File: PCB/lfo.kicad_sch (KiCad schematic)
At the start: 12 parts, among them J4 LFO, U2 LM324

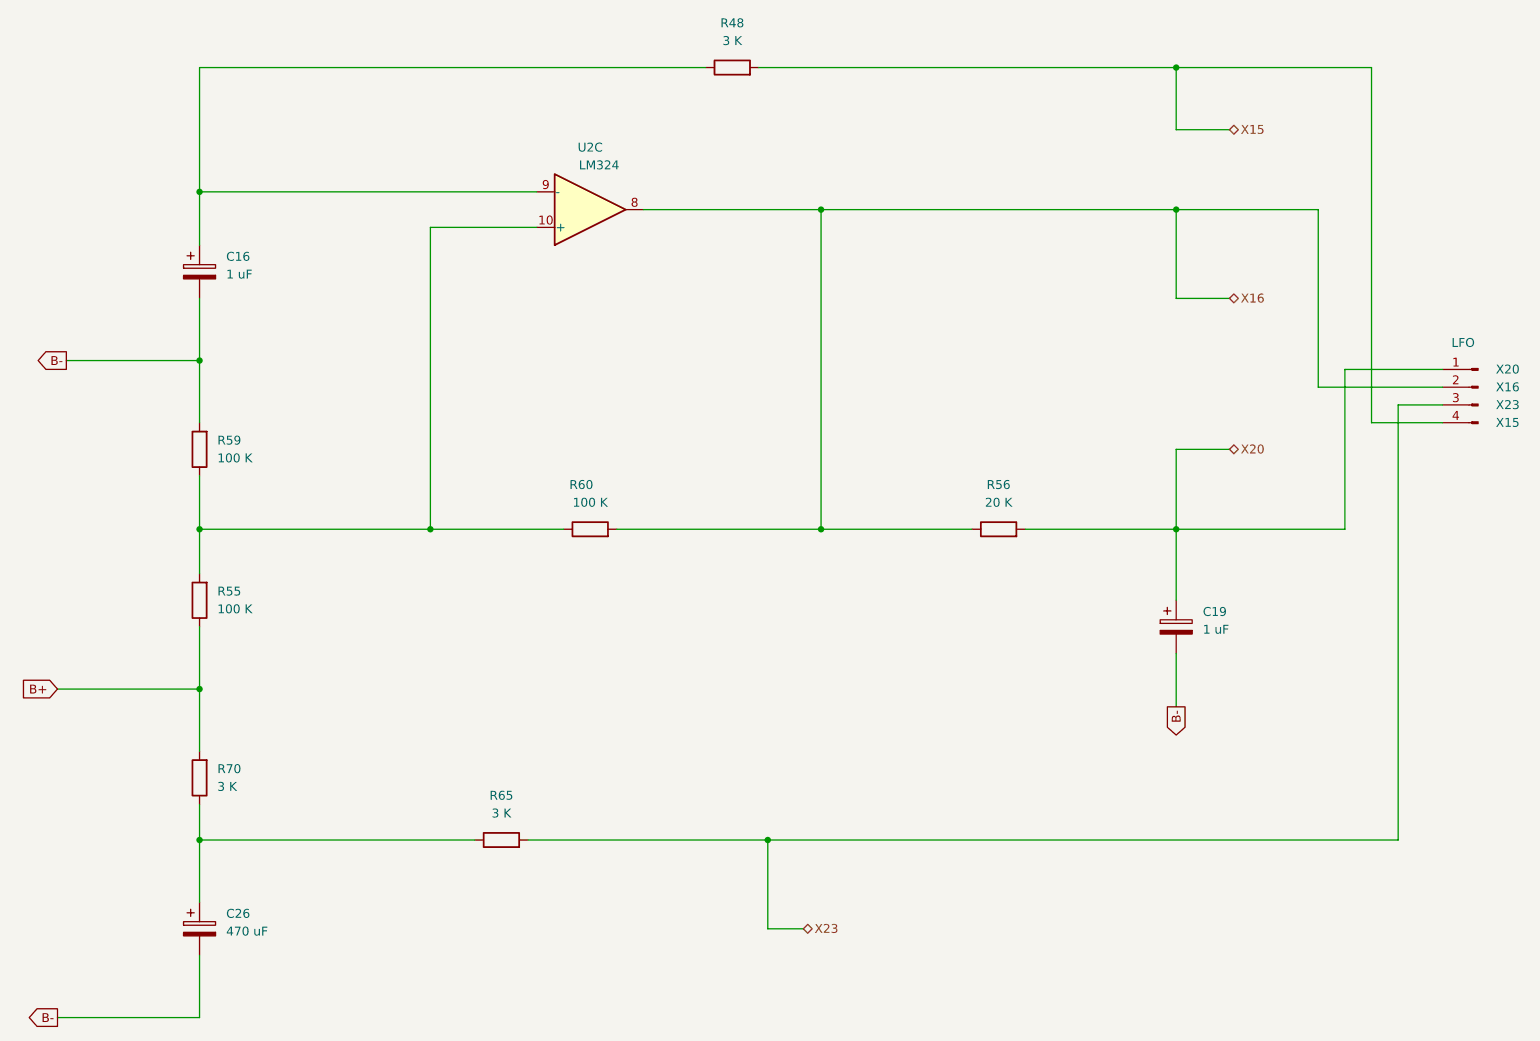
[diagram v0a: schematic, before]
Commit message: Change TO-92 transistors to wide package to avoid shorting during soldering
Added B- hole for speaker
Added more vias to shorten traces
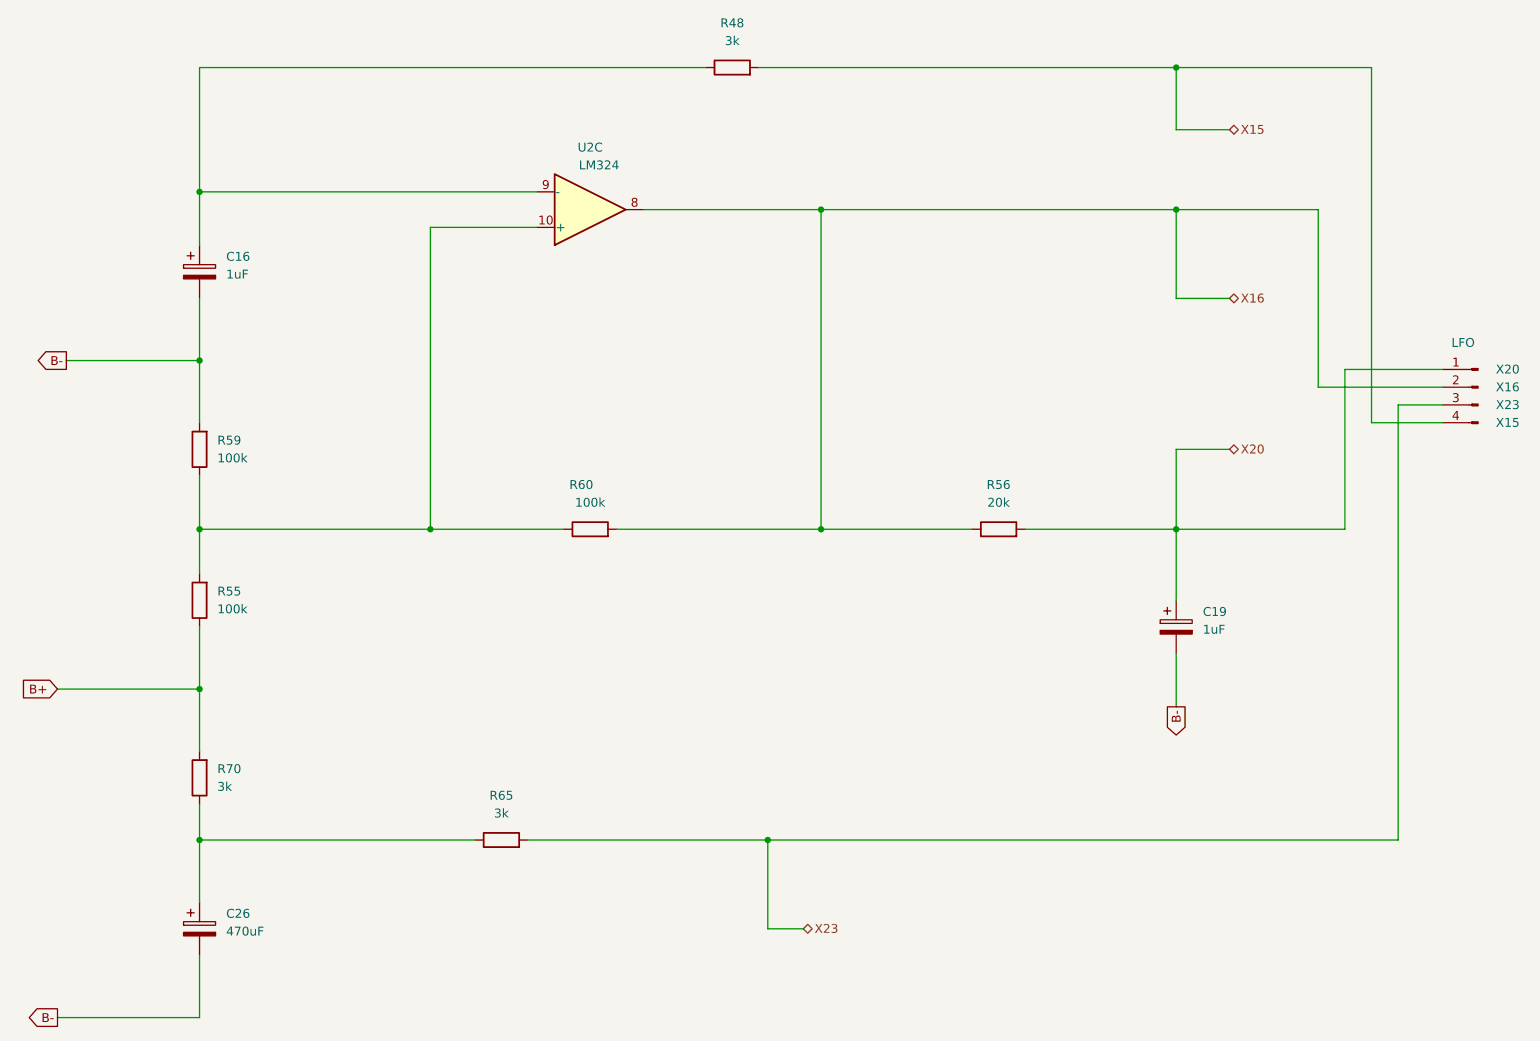
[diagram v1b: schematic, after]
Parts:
- C16, C19: value 1 uF -> 1uF
- C26: value 470 uF -> 470uF
- R48, R65, R70: value 3 K -> 3k
- R55, R59, R60: value 100 K -> 100k
- R56: value 20 K -> 20k
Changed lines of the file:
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@@
 			)
 		)
-		(property "Value" "3 K"
+		(property "Value" "3k"
 			(at 106.68 148.59 90)
 			(show_name no)
@@
 		(fields_autoplaced yes)
 		(property "Reference" "R55"
-			(at 66.04 116.84 0)
-			(show_name no)
-			(do_not_autoplace no)
-			(effects
-				(font
-					(size 1.27 1.27)
-				)
-				(justify right)
-			)
-		)
-		(property "Value" "100 K"
-			(at 66.04 119.38 0)
+			(at 66.04 116.8399 0)
+			(show_name no)
+			(do_not_autoplace no)
+			(effects
+				(font
+					(size 1.27 1.27)
+				)
+				(justify right)
+			)
+		)
+		(property "Value" "100k"
+			(at 66.04 119.3799 0)
 			(show_name no)
 			(do_not_autoplace no)
@@
 		(fields_autoplaced yes)
 		(property "Reference" "R59"
-			(at 66.04 95.25 0)
-			(show_name no)
-			(do_not_autoplace no)
-			(effects
-				(font
-					(size 1.27 1.27)
-				)
-				(justify right)
-			)
-		)
-		(property "Value" "100 K"
-			(at 66.04 97.79 0)
+			(at 66.04 95.2499 0)
+			(show_name no)
+			(do_not_autoplace no)
+			(effects
+				(font
+					(size 1.27 1.27)
+				)
+				(justify right)
+			)
+		)
+		(property "Value" "100k"
+			(at 66.04 97.7899 0)
 			(show_name no)
 			(do_not_autoplace no)
@@
 			)
 		)
-		(property "Value" "100 K"
+		(property "Value" "100k"
 			(at 119.38 104.14 90)
 			(show_name no)
@@
 		(fields_autoplaced yes)
 		(property "Reference" "C19"
-			(at 207.01 119.761 0)
+			(at 207.01 119.7609 0)
 			(show_name no)
 			(do_not_autoplace no)
@@
 			)
 		)
-		(property "Value" "1 uF"
-			(at 207.01 122.301 0)
+		(property "Value" "1uF"
+			(at 207.01 122.3009 0)
 			(show_name no)
 			(do_not_autoplace no)
@@
 			)
 		)
-		(property "Value" "3 K"
+		(property "Value" "3k"
 			(at 139.7 38.1 90)
 			(show_name no)
@@
 		(fields_autoplaced yes)
 		(property "Reference" "C26"
-			(at 67.31 162.941 0)
+			(at 67.31 162.9409 0)
 			(show_name no)
 			(do_not_autoplace no)
@@
 			)
 		)
-		(property "Value" "470 uF"
-			(at 67.31 165.481 0)
+		(property "Value" "470uF"
+			(at 67.31 165.4809 0)
 			(show_name no)
 			(do_not_autoplace no)
@@
 		(fields_autoplaced yes)
 		(property "Reference" "R70"
-			(at 66.04 142.24 0)
-			(show_name no)
-			(do_not_autoplace no)
-			(effects
-				(font
-					(size 1.27 1.27)
-				)
-				(justify right)
-			)
-		)
-		(property "Value" "3 K"
-			(at 66.04 144.78 0)
+			(at 66.04 142.2399 0)
+			(show_name no)
+			(do_not_autoplace no)
+			(effects
+				(font
+					(size 1.27 1.27)
+				)
+				(justify right)
+			)
+		)
+		(property "Value" "3k"
+			(at 66.04 144.7799 0)
 			(show_name no)
 			(do_not_autoplace no)
@@
 		(fields_autoplaced yes)
 		(property "Reference" "C16"
-			(at 67.31 68.961 0)
+			(at 67.31 68.9609 0)
 			(show_name no)
 			(do_not_autoplace no)
@@
 			)
 		)
-		(property "Value" "1 uF"
-			(at 67.31 71.501 0)
+		(property "Value" "1uF"
+			(at 67.31 71.5009 0)
 			(show_name no)
 			(do_not_autoplace no)
@@
 			)
 		)
-		(property "Value" "20 K"
+		(property "Value" "20k"
 			(at 177.8 104.14 90)
 			(show_name no)

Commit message: Necessary Changes to Schematic and PCB
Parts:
- C26: footprint Capacitor_THT:CP_Radial_D14.0mm_P5.00mm -> Capacitor_THT:CP_Radial_D10.0mm_P5.00mm
- J4: footprint Connector_PinHeader_2.00mm:PinHeader_1x04_P2.00mm_Vertical -> Connector_PinSocket_2.54mm:PinSocket_1x04_P2.54mm_Vertical
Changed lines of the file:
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@@
 			)
 		)
-		(property "Footprint" "Connector_PinHeader_2.00mm:PinHeader_1x04_P2.00mm_Vertical"
+		(property "Footprint" "Connector_PinSocket_2.54mm:PinSocket_1x04_P2.54mm_Vertical"
 			(at 246.38 87.63 0)
 			(hide yes)
@@
 			)
 		)
-		(property "Footprint" "Capacitor_THT:CP_Radial_D14.0mm_P5.00mm"
+		(property "Footprint" "Capacitor_THT:CP_Radial_D10.0mm_P5.00mm"
 			(at 64.4652 168.91 0)
 			(hide yes)
